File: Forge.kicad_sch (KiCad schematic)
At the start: 0 parts

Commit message: Added MCU
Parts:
- added U1: STM32F301C6Tx, Package_QFP:LQFP-48_7x7mm_P0.5mm, symbol MCU_ST_STM32F3:STM32F301C6Tx
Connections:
- new net: U1.23 (VSS), U1.35 (VSS), U1.47 (VSS)
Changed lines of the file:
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@@
 	(generator_version "10.0")
 	(paper "A4")
+	(symbol
+		(lib_id "MCU_ST_STM32F3:STM32F301C6Tx")
+		(at 125.73 88.9 0)
+		(unit 1)
+		(body_style 1)
+		(exclude_from_sim no)
+		(in_bom yes)
+		(on_board yes)
+		(in_pos_files yes)
+		(dnp no)
+		(fields_autoplaced yes)
+		(property "Reference" "U1"
+			(at 130.4133 129.54 0)
+			(show_name no)
+			(do_not_autoplace no)
+			(effects
+				(font
+					(size 1.27 1.27)
+				)
+				(justify left)
+			)
+		)
+		(property "Value" "STM32F301C6Tx"
+			(at 130.4133 132.08 0)
+			(show_name no)
+			(do_not_autoplace no)
+			(effects
+				(font
+					(size 1.27 1.27)
+				)
+				(justify left)
+			)
+		)
+		(property "Footprint" "Package_QFP:LQFP-48_7x7mm_P0.5mm"
+			(at 110.49 127 0)
+			(hide yes)
+			(show_name no)
+			(do_not_autoplace no)
+			(effects
+				(font
+					(size 1.27 1.27)
+				)
+				(justify right)
+			)
+		)
+		(property "Datasheet" "https://www.st.com/resource/en/datasheet/stm32f301c6.pdf"
+			(at 125.73 88.9 0)
+			(hide yes)
+			(show_name no)
+			(do_not_autoplace no)
+			(effects
+				(font
+					(size 1.27 1.27)
+				)
+			)
+		)
+		(property "Description" "STMicroelectronics Arm Cortex-M4 MCU, 32KB flash, 16KB RAM, 72 MHz, 2.0-3.6V, 37 GPIO, LQFP48"
+			(at 125.73 88.9 0)
+			(hide yes)
+			(show_name no)
+			(do_not_autoplace no)
+			(effects
+				(font
+					(size 1.27 1.27)
+				)
+			)
+		)
+		(pin "5"
+		)
+		(pin "24"
+		)
+		(pin "16"
+		)
+		(pin "27"
+		)
+		(pin "18"
+		)
+		(pin "23"
+		)
+		(pin "14"
+		)
+		(pin "2"
+		)
+		(pin "3"
+		)
+		(pin "12"
+		)
+		(pin "1"
+		)
+		(pin "10"
+		)
+		(pin "4"
+		)
+		(pin "15"
+		)
+		(pin "7"
+		)
+		(pin "9"
+		)
+		(pin "13"
+		)
+		(pin "11"
+		)
+		(pin "17"
+		)
+		(pin "19"
+		)
+		(pin "20"
+		)
+		(pin "6"
+		)
+		(pin "8"
+		)
+		(pin "21"
+		)
+		(pin "22"
+		)
+		(pin "25"
+		)
+		(pin "26"
+		)
+		(pin "43"
+		)
+		(pin "46"
+		)
+		(pin "48"
+		)
+		(pin "30"
+		)
+		(pin "36"
+		)
+		(pin "45"
+		)
+		(pin "28"
+		)
+		(pin "31"
+		)
+		(pin "34"
+		)
+		(pin "35"
+		)
+		(pin "38"
+		)
+		(pin "39"
+		)
+		(pin "42"
+		)
+		(pin "41"
+		)
+		(pin "33"
+		)
+		(pin "37"
+		)
+		(pin "29"
+		)
+		(pin "32"
+		)
+		(pin "40"
+		)
+		(pin "44"
+		)
+		(pin "47"
+		)
+		(instances
+			(project "Forge"
+				(path "/cc84b251-1cc6-40c5-9c20-0aa447476933"
+					(reference "U1")
+					(unit 1)
+				)
+			)
+		)
+	)
 	(sheet_instances
 		(path "/"

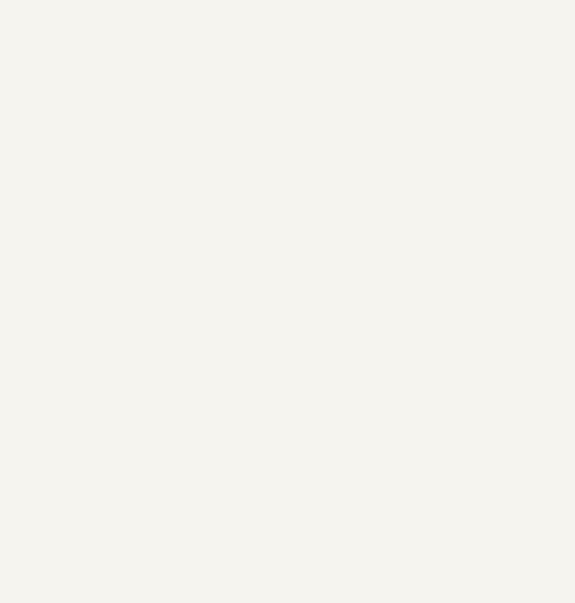
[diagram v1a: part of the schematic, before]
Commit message: Added USB C
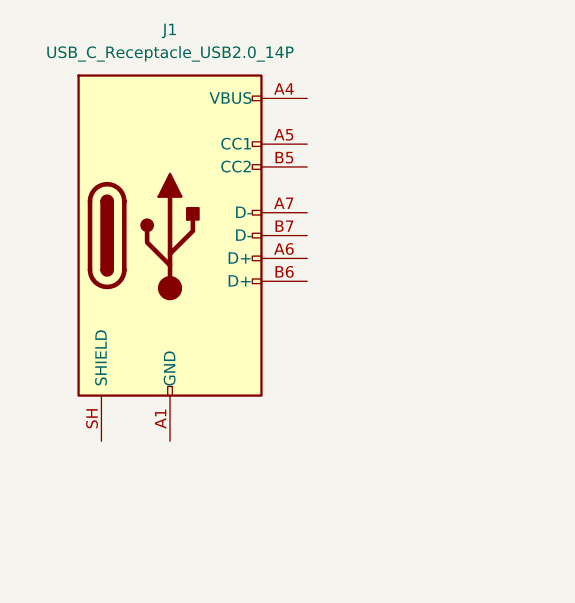
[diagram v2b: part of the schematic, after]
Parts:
- added J1: USB_C_Receptacle_USB2.0_14P, symbol Connector:USB_C_Receptacle_USB2.0_14P
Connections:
- new net: J1.A1 (GND), J1.A12 (GND), J1.B1 (GND), J1.B12 (GND)
- new net: J1.A4 (VBUS), J1.A9 (VBUS), J1.B4 (VBUS), J1.B9 (VBUS)
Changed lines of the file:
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@@
+		)
+	)
+	(symbol
+		(lib_id "Connector:USB_C_Receptacle_USB2.0_14P")
+		(at 31.75 54.61 0)
+		(unit 1)
+		(body_style 1)
+		(exclude_from_sim no)
+		(in_bom yes)
+		(on_board yes)
+		(in_pos_files yes)
+		(dnp no)
+		(fields_autoplaced yes)
+		(property "Reference" "J1"
+			(at 31.75 31.75 0)
+			(show_name no)
+			(do_not_autoplace no)
+			(effects
+				(font
+					(size 1.27 1.27)
+				)
+			)
+		)
+		(property "Value" "USB_C_Receptacle_USB2.0_14P"
+			(at 31.75 34.29 0)
+			(show_name no)
+			(do_not_autoplace no)
+			(effects
+				(font
+					(size 1.27 1.27)
+				)
+			)
+		)
+		(property "Footprint" ""
+			(at 35.56 54.61 0)
+			(hide yes)
+			(show_name no)
+			(do_not_autoplace no)
+			(effects
+				(font
+					(size 1.27 1.27)
+				)
+			)
+		)
+		(property "Datasheet" "https://www.usb.org/sites/default/files/documents/usb_type-c.zip"
+			(at 35.56 54.61 0)
+			(hide yes)
+			(show_name no)
+			(do_not_autoplace no)
+			(effects
+				(font
+					(size 1.27 1.27)
+				)
+			)
+		)
+		(property "Description" "USB 2.0-only 14P Type-C Receptacle connector"
+			(at 31.75 54.61 0)
+			(hide yes)
+			(show_name no)
+			(do_not_autoplace no)
+			(effects
+				(font
+					(size 1.27 1.27)
+				)
+			)
+		)
+		(pin "A1"
+		)
+		(pin "A6"
+		)
+		(pin "B4"
+		)
+		(pin "A4"
+		)
+		(pin "A5"
+		)
+		(pin "A7"
+		)
+		(pin "A9"
+		)
+		(pin "A12"
+		)
+		(pin "B1"
+		)
+		(pin "B7"
+		)
+		(pin "B6"
+		)
+		(pin "B5"
+		)
+		(pin "B9"
+		)
+		(pin "SH"
+		)
+		(pin "B12"
+		)
+		(instances
+			(project "Forge"
+				(path "/cc84b251-1cc6-40c5-9c20-0aa447476933"
+					(reference "J1")
+					(unit 1)
+				)
+			)
 		)
 	)

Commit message: Started schematic and pcb
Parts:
- J1: footprint (none) -> Connector_USB:USB_C_Receptacle_GCT_USB4105-xx-A_16P_TopMnt_Horizontal
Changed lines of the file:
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@@
 			)
 		)
-		(property "Footprint" ""
+		(property "Footprint" "Connector_USB:USB_C_Receptacle_GCT_USB4105-xx-A_16P_TopMnt_Horizontal"
 			(at 35.56 54.61 0)
 			(hide yes)

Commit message: Began basic power design
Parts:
- added R1, R2: 5k1, Resistor_SMD:R_0805_2012Metric_Pad1.20x1.40mm_HandSolder, symbol Device:R
- added U2: AP2112K-3.3, Package_TO_SOT_SMD:SOT-23-5, symbol Regulator_Linear:AP2112K-3.3
- added U3: USBLC6-2SC6, Package_TO_SOT_SMD:SOT-23-6, symbol Power_Protection:USBLC6-2SC6
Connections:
- net GND: now reaches J1.A1 (GND), J1.A12 (GND), J1.B1 (GND), J1.B12 (GND)
- net GND: now also R1.2, R2.2, U3.2 (GND)
- net +5V: now reaches J1.A4 (VBUS), J1.A9 (VBUS), J1.B4 (VBUS), J1.B9 (VBUS)
- net +5V: now also U3.5 (VBUS)
- net CC1: now reaches J1.A5 (CC1)
- net CC1: now also R1.1
- net USB_Conn_D-: now reaches J1.A6 (D+)
- net USB_Conn_D-: now also J1.B6 (D+), U3.6 (I/O1)
- net USB_Conn_D+: now reaches J1.A7 (D-)
- net USB_Conn_D+: now also J1.B7 (D-), U3.1 (I/O1)
- net CC2: now reaches J1.B5 (CC2)
- net CC2: now also R2.1
- new net USB_D+: U3.3 (I/O2)
- new net USB_D-: U3.4 (I/O2)
- no-connect marks 0 -> 1
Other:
- moved on the sheet: U1

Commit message: Changed to MCU from stm32 to esp32 wroom for easier use for a first board
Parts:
- removed U1: STM32F301C6Tx, Package_QFP:LQFP-48_7x7mm_P0.5mm, symbol MCU_ST_STM32F3:STM32F301C6Tx
- added C1, C2: 1u, Capacitor_SMD:C_0805_2012Metric_Pad1.18x1.45mm_HandSolder, symbol Device:C
- added C3: 100n, Capacitor_SMD:C_0805_2012Metric_Pad1.18x1.45mm_HandSolder, symbol Device:C
- added C4: 10u, Capacitor_SMD:C_0805_2012Metric_Pad1.18x1.45mm_HandSolder, symbol Device:C
- added U1: ESP32-S3-WROOM-2, RF_Module:ESP32-S3-WROOM-2, symbol RF_Module:ESP32-S3-WROOM-2
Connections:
- net +5V: now also U2.1 (VIN), U2.3 (EN), C1.1
- net GND: now also U2.2 (GND), C1.2, C2.2, C3.2, C4.2, U1.1 (GND), U1.40 (GND), U1.41 (GND)
- net USB_D+: now also U1.14 (USB_D+/IO20)
- net USB_D-: now also U1.13 (USB_D-/IO19)
- net +3.3V: now reaches U2.5 (VOUT)
- net +3.3V: now also C2.1, C3.1, C4.1, U1.2 (3V3)
- new net I2C_SCL: U1.17 (IO9)
- new net I2C_SDA: U1.12 (IO8)
- new net SPI_CLK: U1.18 (IO10)
- new net SPI_CS: U1.21 (IO13)
- new net SPI_MISO: U1.20 (IO12)
- new net SPI_MOSI: U1.19 (IO11)

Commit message: Finished schematic ready for review
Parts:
- removed U1: ESP32-S3-WROOM-2, RF_Module:ESP32-S3-WROOM-2, symbol RF_Module:ESP32-S3-WROOM-2
- added C5, C6: 100n, Capacitor_SMD:C_0805_2012Metric_Pad1.18x1.45mm_HandSolder, symbol Device:C
- added C7: 10u, Capacitor_SMD:C_0805_2012Metric_Pad1.18x1.45mm_HandSolder, symbol Device:C
- added C8, C9: 100n, Capacitor_SMD:C_0603_1608Metric_Pad1.08x0.95mm_HandSolder, symbol Device:C
- added J2: SWD, Connector_PinHeader_2.54mm:PinHeader_1x05_P2.54mm_Vertical, symbol Connector:Conn_01x05_Pin
- added J3: SPI, Connector_PinHeader_2.54mm:PinHeader_1x06_P2.54mm_Vertical, symbol Connector:Conn_01x06_Pin
- added J4: I2C, Connector_PinHeader_2.54mm:PinHeader_1x04_P2.54mm_Vertical, symbol Connector:Conn_01x04_Pin
- added U1: STM32F042K6Tx, Package_QFP:LQFP-32_7x7mm_P0.8mm, symbol MCU_ST_STM32F0:STM32F042K6Tx
- added Y1: Crystal_GND24, Crystal:Crystal_SMD_EuroQuartz_MT-4Pin_3.2x2.5mm_HandSoldering, symbol Device:Crystal_GND24
- C4: value 10u -> 100n
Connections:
- net +3.3V: now also C5.1, C6.1, C7.1, J2.1 (Pin_1), J3.1 (Pin_1), J4.1 (Pin_1), U1.1 (VDD), U1.17 (VDDIO2), U1.5 (VDDA); no longer C3.1
- net GND: now also C5.2, C6.2, C7.2, C8.2, C9.2, J2.5 (Pin_5), J3.6 (Pin_6), J4.4 (Pin_4), U1.16 (VSS), U1.32 (VSSA), Y1.2 (G), Y1.4 (G)
- net I2C_SCL: now also J4.2 (Pin_2), U1.29 (PB6)
- net I2C_SDA: now also J4.3 (Pin_3), U1.30 (PB7)
- net SPI_MISO: now also J3.4 (Pin_4), U1.12 (PA6)
- net SPI_MOSI: now also J3.5 (Pin_5), U1.13 (PA7)
- net USB_D+: now also U1.22 (PA12)
- net USB_D-: now also U1.21 (PA11)
- new net BOOT0: U1.31 (PB8)
- new net NRST: C3.1, J2.4 (Pin_4), U1.4 (NRST)
- new net OSC_IN: C8.1, U1.2 (PF0), Y1.1
- new net OSC_OUT: C9.1, U1.3 (PF1), Y1.3
- new net SPI_NSS: J3.2 (Pin_2), U1.10 (PA4)
- new net SPI_SCK: J3.3 (Pin_3), U1.11 (PA5)
- new net SWCLK: J2.3 (Pin_3), U1.24 (PA14)
- new net SWDIO: J2.2 (Pin_2), U1.23 (PA13)
- no-connect marks 1 -> 13

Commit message: Components placed based on the schematic layout
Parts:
- added J5: Boot0, Connector_PinHeader_2.54mm:PinHeader_1x02_P2.54mm_Vertical, symbol Connector:Conn_01x02_Pin
- added R3: 10k, Resistor_SMD:R_0805_2012Metric_Pad1.20x1.40mm_HandSolder, symbol Device:R
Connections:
- net +3.3V: now also J2.5 (Pin_5), J3.6 (Pin_6), J4.4 (Pin_4), J5.2 (Pin_2); no longer J2.1 (Pin_1), J3.1 (Pin_1), J4.1 (Pin_1)
- net BOOT0: now also J5.1 (Pin_1), R3.2
- net GND: now also J2.1 (Pin_1), J3.1 (Pin_1), J4.1 (Pin_1), R3.1; no longer J2.5 (Pin_5), J3.6 (Pin_6), J4.4 (Pin_4)
- net I2C_SCL: now also J4.3 (Pin_3); no longer J4.2 (Pin_2)
- net I2C_SDA: now also J4.2 (Pin_2); no longer J4.3 (Pin_3)
- net NRST: now also J2.2 (Pin_2); no longer J2.4 (Pin_4)
- net SPI_MISO: now also J3.3 (Pin_3); no longer J3.4 (Pin_4)
- net SPI_MOSI: now also J3.2 (Pin_2); no longer J3.5 (Pin_5)
- net SPI_NSS: now also J3.5 (Pin_5); no longer J3.2 (Pin_2)
- net SPI_SCK: now also J3.4 (Pin_4); no longer J3.3 (Pin_3)
- net SWDIO: now also J2.4 (Pin_4); no longer J2.2 (Pin_2)
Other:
- moved on the sheet: J2, J3, J4
